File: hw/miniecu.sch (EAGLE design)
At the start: 60 parts

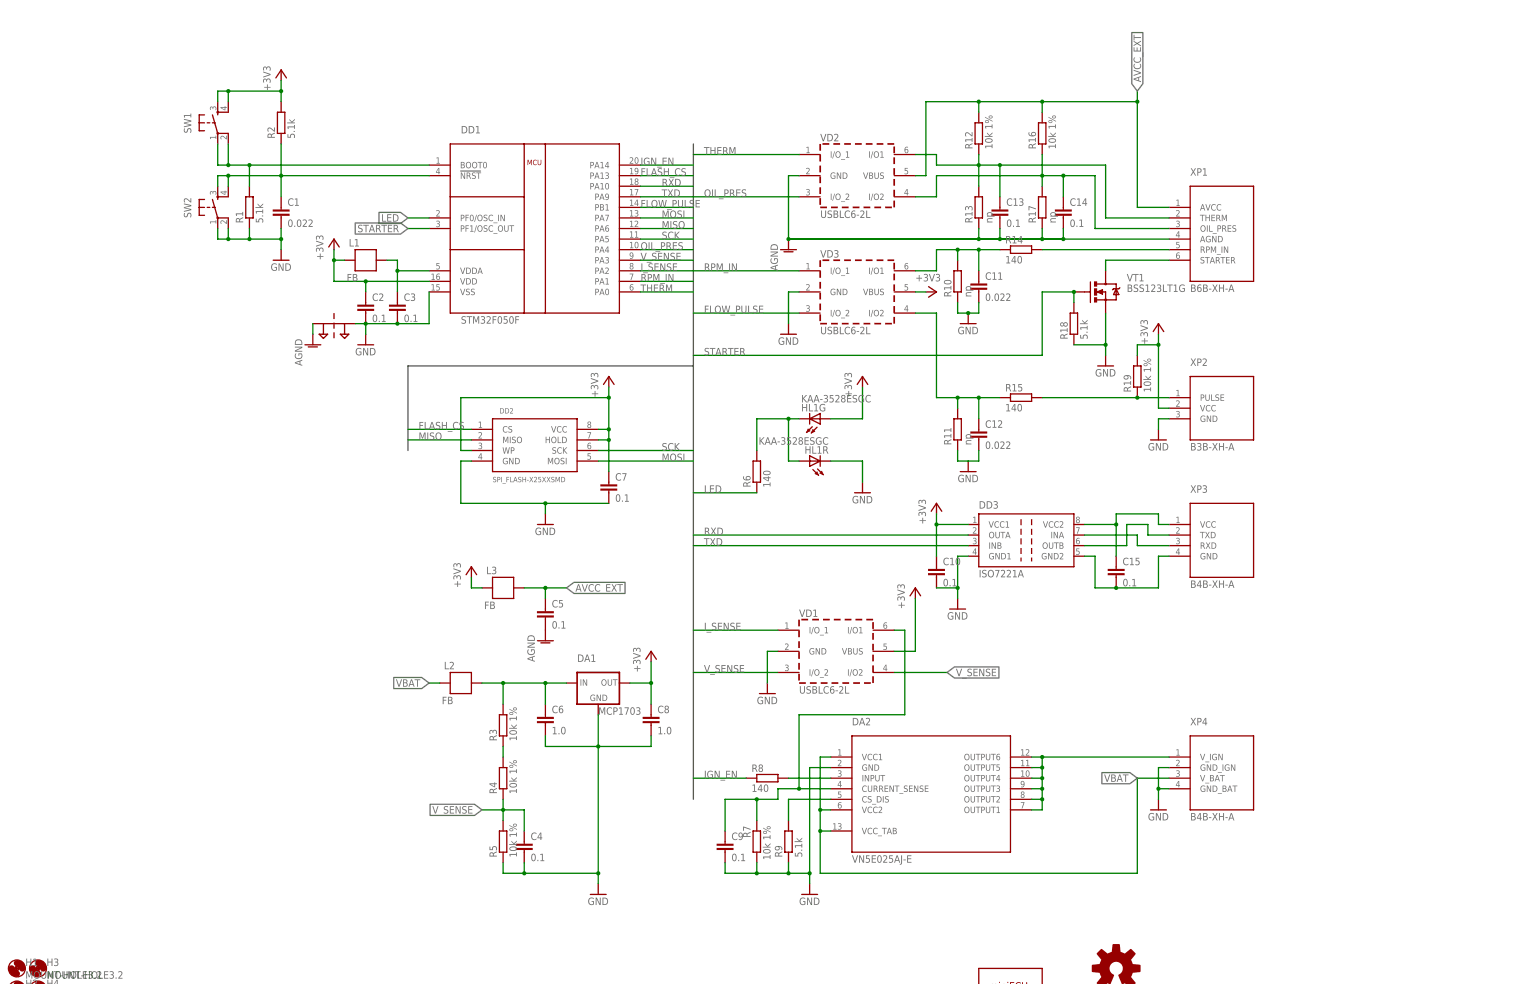
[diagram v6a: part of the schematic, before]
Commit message: hw: replace mcu
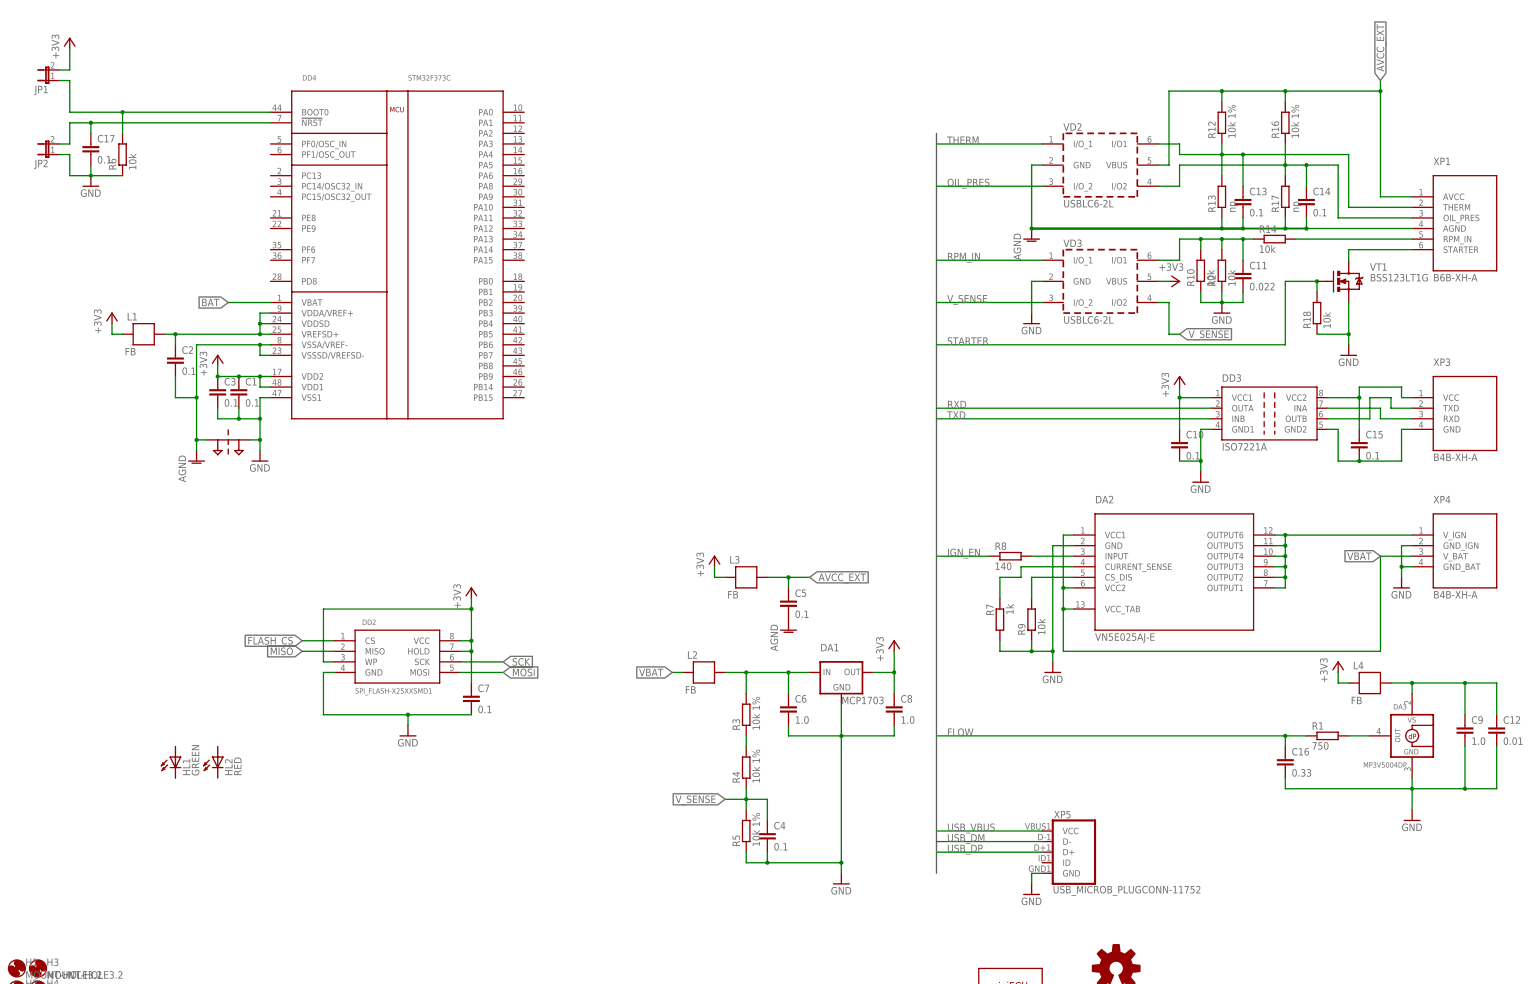
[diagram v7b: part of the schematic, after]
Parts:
- removed DD1: STM32F050F, stm32f050:STM32F050F
- removed R11: np, resistor:R-EU_R0603
- removed R15: 140, resistor:R-EU_R0603
- removed R19: 10k 1%, resistor:R-EU_R0805
- removed SW1, SW2: (no value), SparkFun-Electromechanical:TAC_SWITCHSMD
- removed VD1: USBLC6-2L, usblc6:USBLC6-2SC6
- removed XP2: B3B-XH-A, miniecu-con:FLOW_SENS-B3B-XH-A
- added C16: 0.33, resistor:C-EUC0603
- added C17: 0.1, resistor:C-EUC0603
- added DA3: MP3V5004DP, microbuilder:MPXV7025DP
- added DD4: STM32F373C, stm32f373:STM32F373C
- added HL2: RED, SparkFun-LED:LED-RED0603
- added JP1, JP2: (no value), SparkFun-Passives:JUMPER-2SMD-NO
- added L4: FB, SparkFun-Passives:FB
- added XP5: USB_MICROB_PLUGCONN-11752, SparkFun-Connectors:USB_MICROB_PLUGCONN-11752
- C1: value 0.022 -> 0.1
- C12: value 0.022 -> 0.01
- C9: value 0.1 -> 1.0; device resistor:C-EUC0603 -> resistor:C-EUC0805
- DD2: value SPI_FLASH-X25XXSMD -> SPI_FLASH-X25XXSMD1; device SparkFun-DigitalIC:SPI_FLASH-X25XXSMD -> SparkFun-DigitalIC:SPI_FLASH-X25XXSMD1
- HL1: value KAA-3528ESGC -> GREEN; device led2:KAA-3528ESGC -> SparkFun-LED:LED-GREEN0603
- R1: value 5.1k -> 750
- R10: value np -> 10k
- R14, R6: value 140 -> 10k
- R18, R2, R9: value 5.1k -> 10k
- R7: value 10k 1% -> 1k; device resistor:R-EU_R0805 -> resistor:R-EU_R0603
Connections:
- removed net !NRST: C1.1, DD1.!NRST, R2.1, SW2.3, SW2.4
- removed net AVCC: C3.1, DD1.VDDA, L1.P$1
- removed net BOOT0: DD1.BOOT0, R1.2, SW1.1, SW1.2
- removed net FLOW_PULSE: C12.1, DD1.PB1, R11.2, R15.1, VD3.I/O2, VD3.I/O_2
- removed net I_SENSE: C9.1, DA2.CURRENT_SENSE, DD1.PA2, R7.1, VD1.I/O1, VD1.I/O_1
- removed net LED: DD1.PF0/OSC_IN, R6.1
- new net BAT: DD4.VBAT
- new net FLOW: C16.1, R1.1
- new net N$10: C17.1, DD4.!NRST, JP2.2
- new net N$11: DD4.BOOT0, JP1.1, R6.2
- new net N$3: C12.1, C9.1, DA3.VS, L4.P$1
- new net N$5: C2.1, DD4.VDDA/VREF+, DD4.VDDSD, DD4.VREFSD+, L1.P$1
- new net USB_DM: XP5.D-
- new net USB_DP: XP5.D+
- new net USB_VBUS: XP5.VCC
- net +3V3: now also C1.1, C3.1, DD4.VDD1, DD4.VDD2, JP1.2, L4.P$2; no longer C2.1, DD1.VDD, HL1G.A, R19.2, R2.2, SW1.3, SW1.4, VD1.VBUS, XP2.VCC
- net AGND: now also C2.2, DD4.VSSA/VREF-, DD4.VSSSD/VREFSD-
- net FLASH_CS: no longer DD1.PA13
- net GND: now also C16.2, C17.2, DA3.GND, DD4.VSS1, JP2.1, R2.1, R6.1, XP5.GND; no longer C2.2, DD1.VSS, HL1R.C, R1.1, R11.1, SW2.1, SW2.2, VD1.GND, XP2.GND
- net IGN_EN: no longer DD1.PA14
- net MISO: no longer DD1.PA6
- net MOSI: no longer DD1.PA7
- net N$2: now also DA2.CURRENT_SENSE, R7.1; no longer HL1G.C, HL1R.A, R6.2
- net N$4: now also DA3.+VOUT, R1.2; no longer R15.2, R19.1, XP2.PULSE
- net OIL_PRES: no longer DD1.PA4
- net RPM_IN: now also R2.2; no longer DD1.PA1
- net RXD: no longer DD1.PA10
- net SCK: no longer DD1.PA5
- net STARTER: no longer DD1.PF1/OSC_OUT
- net THERM: no longer DD1.PA0
- net TXD: no longer DD1.PA9
- net V_SENSE: now also VD3.I/O2, VD3.I/O_2; no longer DD1.PA3, VD1.I/O2, VD1.I/O_2
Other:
- moved on the sheet: C1, C10, C11, C12, C13, C14, C15, C2, C3, C4, C5, C6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

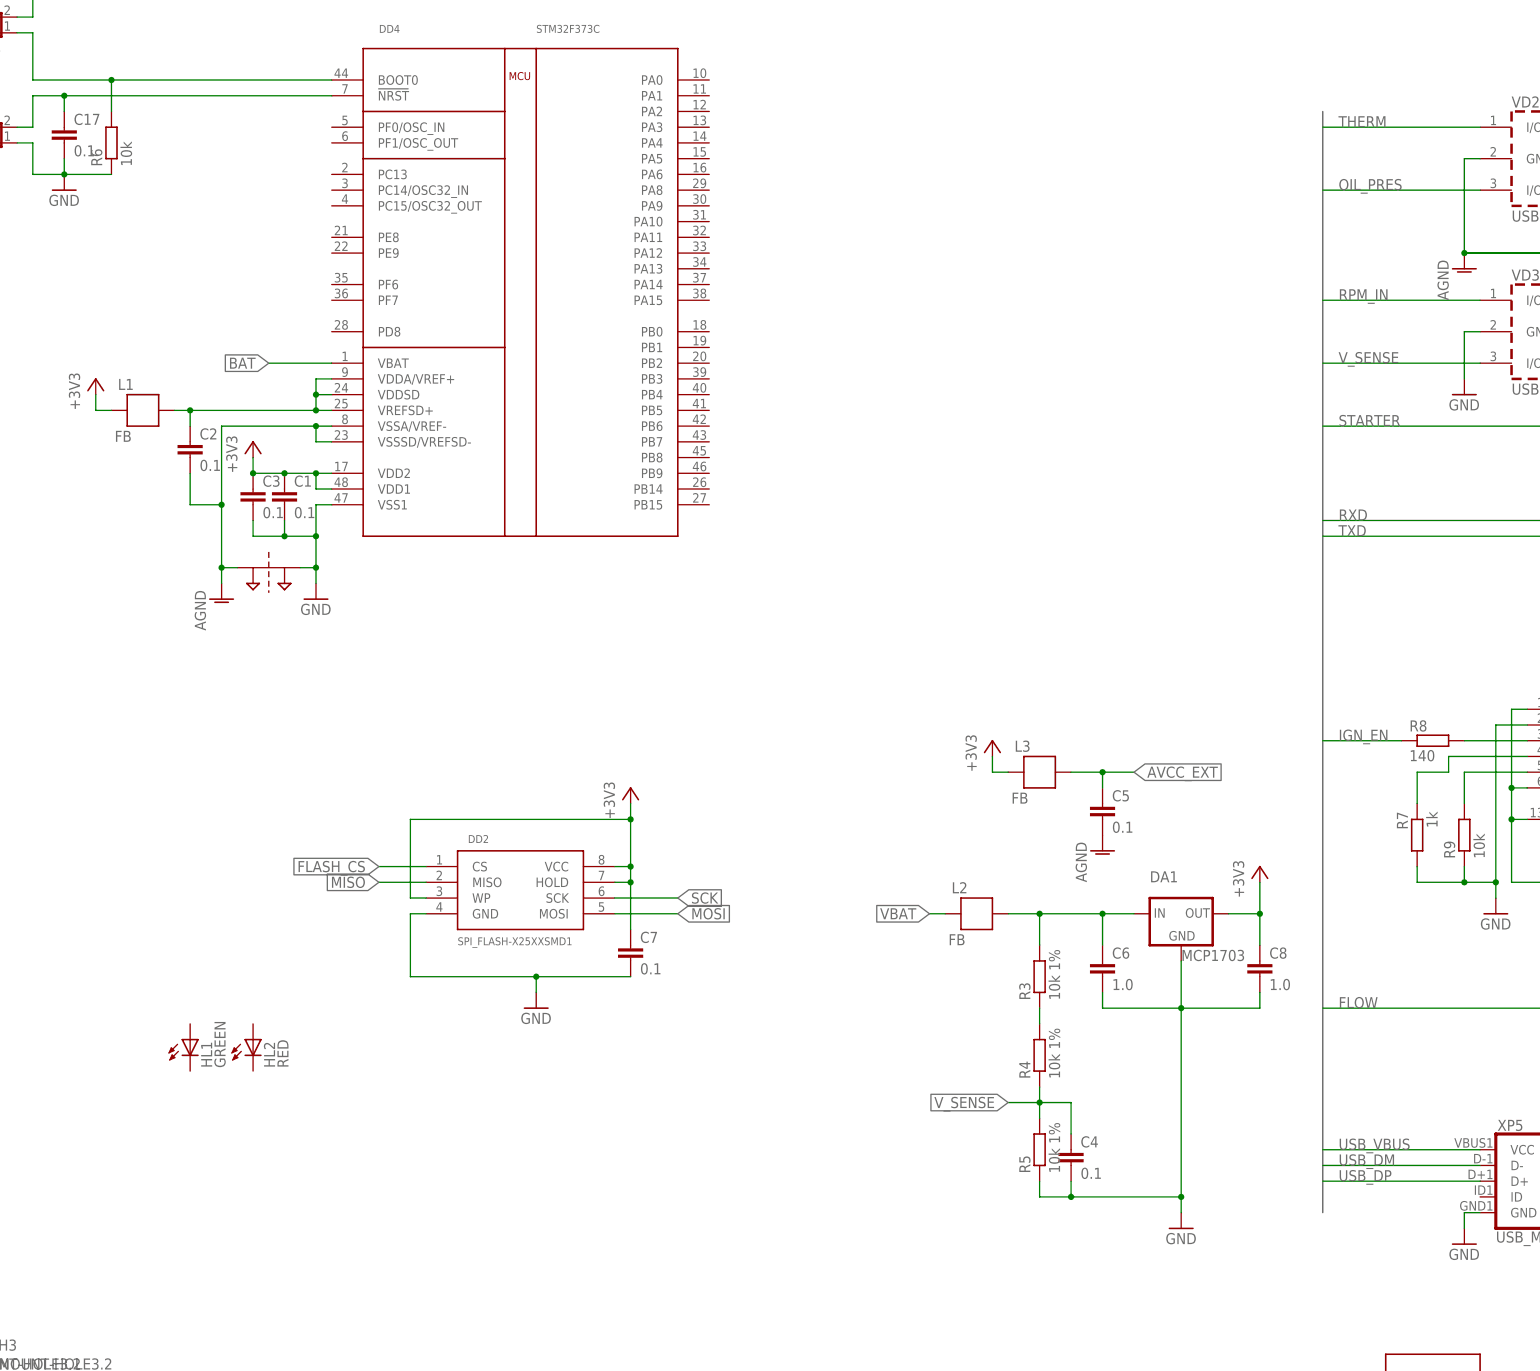
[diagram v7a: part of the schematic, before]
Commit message: hw: add library for Murata CSTCE resonators
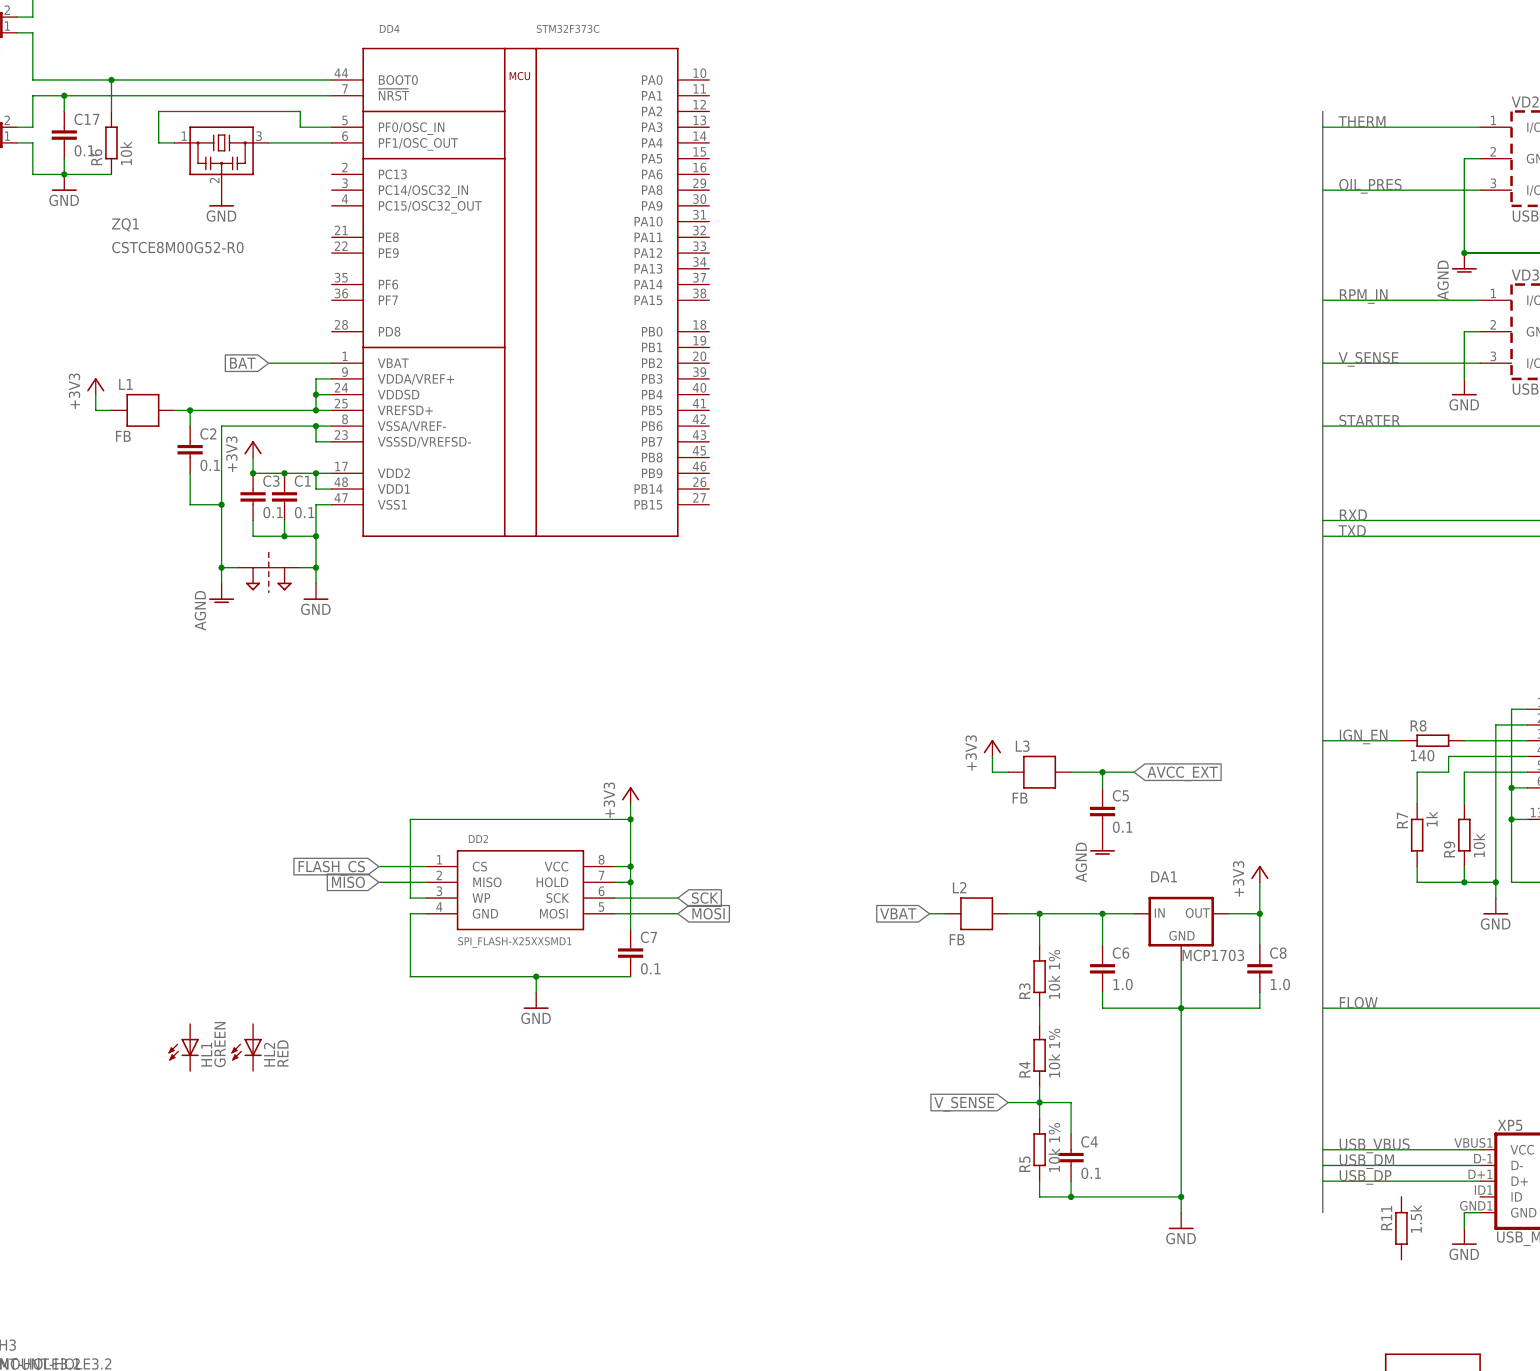
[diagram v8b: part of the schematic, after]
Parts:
- added R11: 1.5k, resistor:R-EU_R0603
- added ZQ1: CSTCE8M00G52-R0, cstce-resonator:CSTCE8M00G52-R0
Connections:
- new net OSC_IN: DD4.PF0/OSC_IN, ZQ1.1
- new net OSC_OUT: DD4.PF1/OSC_OUT, ZQ1.3
- net GND: now also ZQ1.2
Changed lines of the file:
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@@
 <part name="+3V8" library="supply1" deviceset="+3V3" device=""/>
 <part name="GND10" library="supply1" deviceset="GND" device=""/>
+<part name="R11" library="resistor" deviceset="R-EU_" device="R0603" value="1.5k"/>
+<part name="ZQ1" library="cstce-resonator" deviceset="CSTC?" device="E" technology="8M00G52-R0"/>
+<part name="GND12" library="supply1" deviceset="GND" device=""/>
 </parts>
 <sheets>
@@
 <instance part="+3V8" gate="G$1" x="-114.3" y="53.34"/>
 <instance part="GND10" gate="1" x="-109.22" y="17.78"/>
+<instance part="R11" gate="G$1" x="106.68" y="-149.86" rot="MR270"/>
+<instance part="ZQ1" gate="G$1" x="-83.82" y="25.4" smashed="yes">
+<attribute name="NAME" x="-101.6" y="11.43" size="1.778" layer="95"/>
+<attribute name="VALUE" x="-101.6" y="7.62" size="1.778" layer="96"/>
+</instance>
+<instance part="GND12" gate="1" x="-83.82" y="15.24"/>
 </instances>
 <busses>
@@
 <junction x="-109.22" y="20.32"/>
 <pinref part="GND10" gate="1" pin="GND"/>
+</segment>
+<segment>
+<pinref part="ZQ1" gate="G$1" pin="2"/>
+<pinref part="GND12" gate="1" pin="GND"/>
 </segment>
 </net>
@@
 </segment>
 </net>
+<net name="OSC_OUT" class="0">
+<segment>
+<pinref part="DD4" gate="G$1" pin="PF1/OSC_OUT"/>
+<pinref part="ZQ1" gate="G$1" pin="3"/>
+<wire x1="-66.04" y1="25.4" x2="-76.2" y2="25.4" width="0.1524" layer="91"/>
+</segment>
+</net>
+<net name="OSC_IN" class="0">
+<segment>
+<pinref part="DD4" gate="G$1" pin="PF0/OSC_IN"/>
+<wire x1="-66.04" y1="27.94" x2="-71.12" y2="27.94" width="0.1524" layer="91"/>
+<wire x1="-71.12" y1="27.94" x2="-71.12" y2="30.48" width="0.1524" layer="91"/>
+<wire x1="-71.12" y1="30.48" x2="-93.98" y2="30.48" width="0.1524" layer="91"/>
+<wire x1="-93.98" y1="30.48" x2="-93.98" y2="25.4" width="0.1524" layer="91"/>
+<pinref part="ZQ1" gate="G$1" pin="1"/>
+<wire x1="-93.98" y1="25.4" x2="-91.44" y2="25.4" width="0.1524" layer="91"/>
+</segment>
+</net>
